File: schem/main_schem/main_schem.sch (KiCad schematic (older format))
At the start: 0 parts

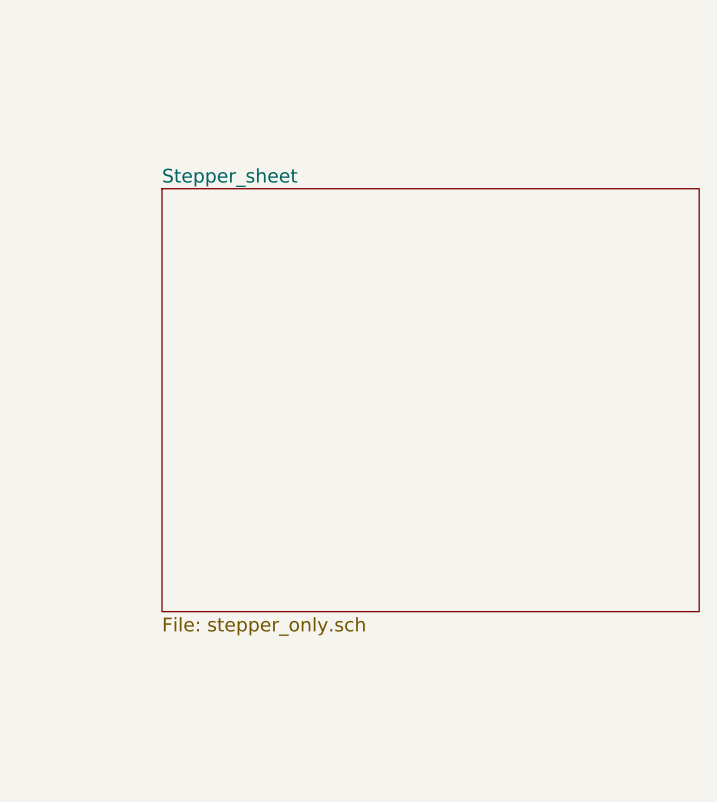
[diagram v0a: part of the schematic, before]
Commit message: Begin board, layout mcu, xtal, eeprom
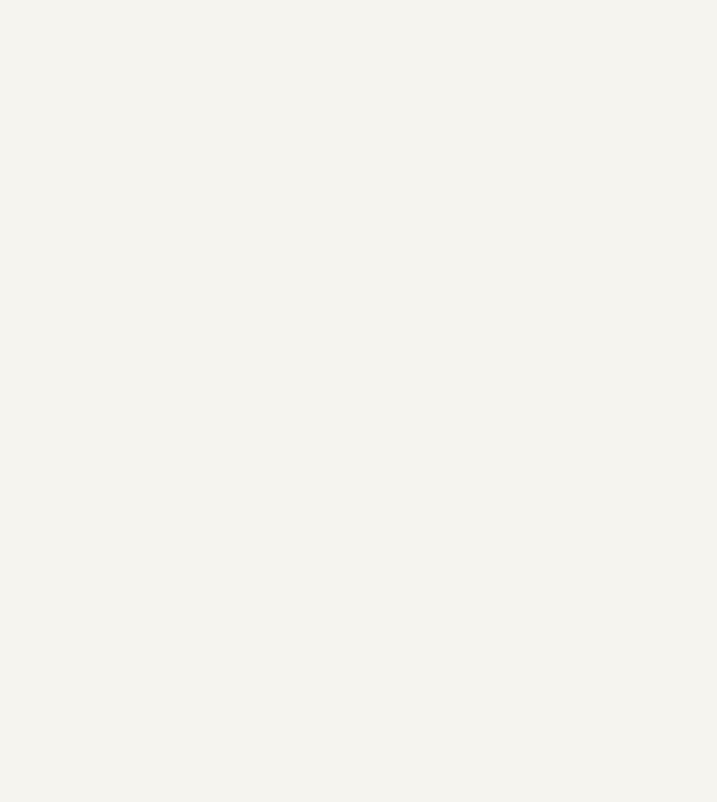
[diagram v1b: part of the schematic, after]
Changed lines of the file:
@@
-EESchema Schematic File Version 2  date 9/29/2012 4:29:19 PM
+EESchema Schematic File Version 2  date 10/1/2012 7:44:23 AM
 LIBS:power
 LIBS:device
@@
 $Descr A4 11700 8267
 encoding utf-8
-Sheet 1 6
+Sheet 1 5
 Title "noname.sch"
-Date "29 sep 2012"
+Date "1 oct 2012"
 Rev "0.1"
 Comp ""
@@
 F1 "NFC.sch" 60
 $EndSheet
-$Sheet
-S 8100 2150 2350 1850
-U 5042EF28
-F0 "Stepper_sheet" 60
-F1 "stepper_only.sch" 60
-$EndSheet
 $EndSCHEMATC

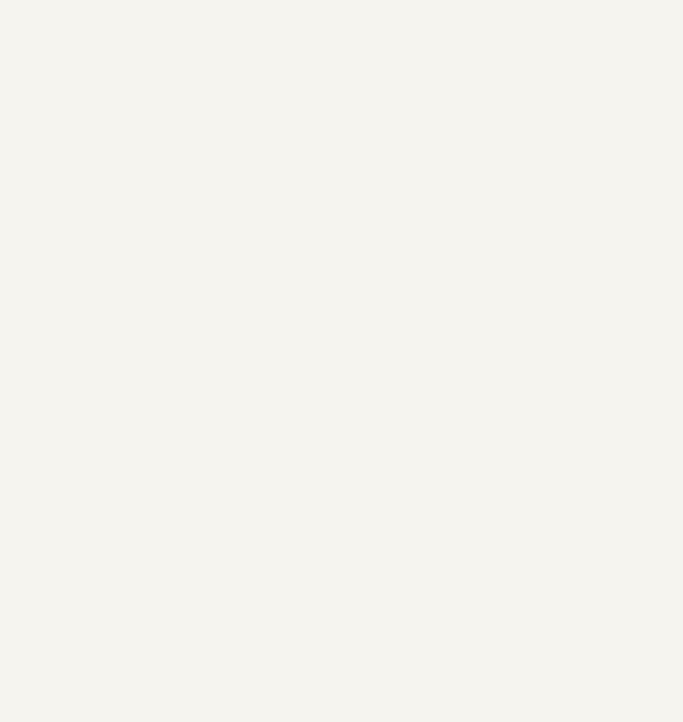
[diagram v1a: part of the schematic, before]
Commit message: Ethernet Anolog, breakout pins, SPI iface breakout for NFC
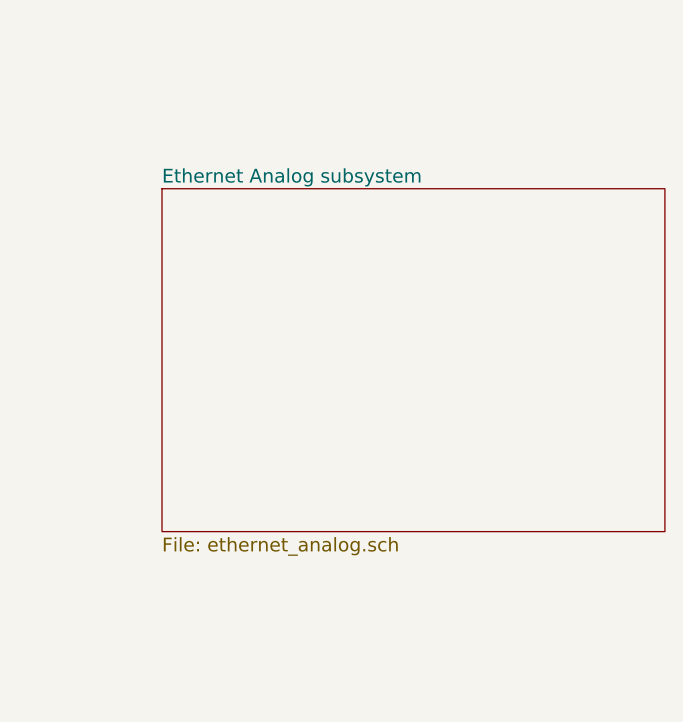
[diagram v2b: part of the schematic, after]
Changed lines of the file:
@@
-EESchema Schematic File Version 2  date 10/1/2012 7:44:23 AM
+EESchema Schematic File Version 2  date 10/5/2012 10:31:23 AM
 LIBS:power
 LIBS:device
@@
 $Descr A4 11700 8267
 encoding utf-8
-Sheet 1 5
+Sheet 1 6
 Title "noname.sch"
-Date "1 oct 2012"
+Date "5 oct 2012"
 Rev "0.1"
 Comp ""
@@
 $EndDescr
 $Sheet
+S 7700 2450 2200 1500
+U 506EEAD1
+F0 "Ethernet Analog subsystem" 60
+F1 "ethernet_analog.sch" 60
+$EndSheet
+$Sheet
 S 4650 850  1700 1250
